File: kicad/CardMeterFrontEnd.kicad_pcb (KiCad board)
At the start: 2 copper layers, 26.7 x 13 mm, 24 parts, among them J1 V+, J2 R-, J3 A+, J4 COM, J5 Analog, J6 Gain, J7 ADC, U1 LTC1992, U2 AD8231, U3 LTC2315

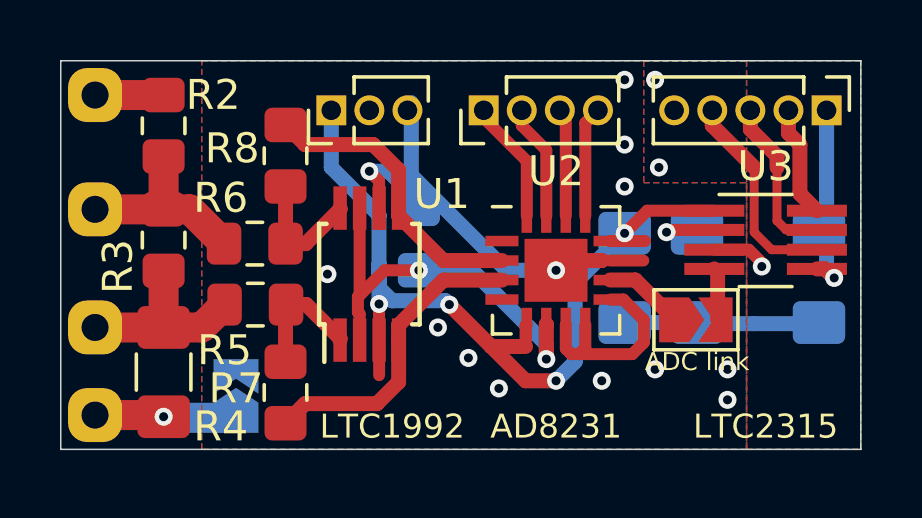
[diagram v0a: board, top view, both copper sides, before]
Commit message: front and is working
Common Mode problem, probably due to resistor matching
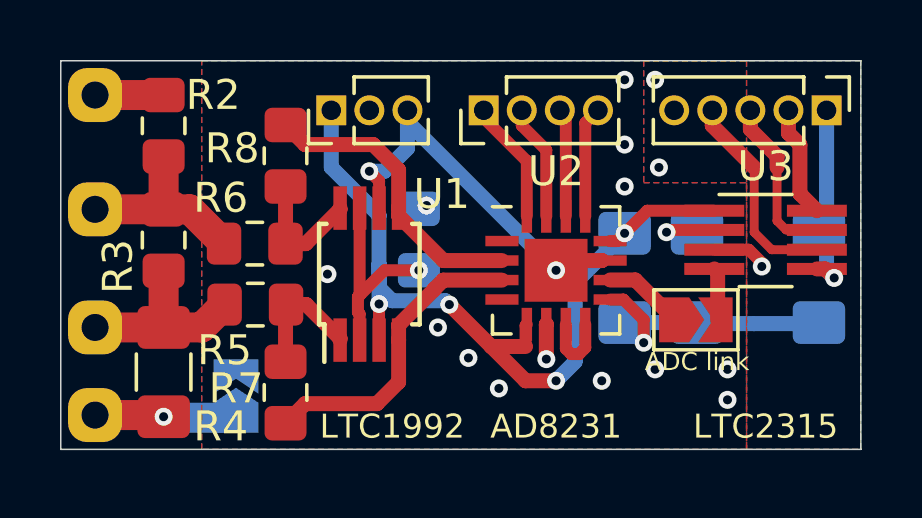
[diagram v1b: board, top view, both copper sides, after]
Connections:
- C1 pad 2: VSSA -> GNDA
- U2 pad 6: Net-(C1-Pad1) -> GNDA
- U2 pad 9: Net-(U2-Pad7) -> GNDA
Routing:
- net Net-(C1-Pad1): track 13.8 -> 6.85 mm, vias 2 -> 1
- net Net-(U2-Pad7): track 6.88 -> 2.40 mm
- net GNDA: track 3.33 -> 6.64 mm, vias 11 -> 14
- net VSSA: track 15.7 -> 12.8 mm
- net VDDA: track 30.3 -> 27.9 mm
